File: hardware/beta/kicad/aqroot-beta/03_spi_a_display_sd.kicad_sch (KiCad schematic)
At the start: 0 parts

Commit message: AQROOT Beta: capture I2C, audio, IR, and SPI-A subsystems
Reconciles the active KiCad project from OneDrive into the canonical
repository. The four subsystem sheets existed here only as 169-byte
empty stubs; the real schematic capture had been done in the OneDrive
working copy.

Sheets brought in:
  03_spi_a_display_sd.kicad_sch   stub ->  62136 bytes
  05_i2c_devices.kicad_sch        stub ->  59631 bytes
  06_audio.kicad_sch              stub ->  55263 bytes
  07_ir.kicad_sch                 stub ->  50216 bytes

Also updated: aqroot-Beta.kicad_sch (root sheet, now carrying the
child sheet instances) and aqroot-Beta.kicad_pro.

03_spi_a_display_sd instantiates AQROOT_Beta:ILI9341_FT6236_MODULE_-
PLACEHOLDER; its cached symbol matches libraries/AQROOT_Beta.kicad_sym
exactly (13 pins, blank footprint, on_board=no).

Deliberately not taken from OneDrive:
  - sym-lib-table / fp-lib-table. The OneDrive copies hard-code an
    absolute P:/ path to this repository's library; the versions kept
    here use ${KIPRJMOD} and stay portable.
  - aqroot-Beta.kicad_prl (local project state) and .history/
    (2388 editor-history files, 5.87 MB).

Sheets identical on both sides and therefore untouched: 01_power_tree,
02_mcu_core, 04_spi_b_radios_nfc, 08_buttons_expanders,
09_community_header, aqroot-Beta.kicad_pcb.

Every copied file was verified by SHA-256 against its source, and each
staged blob is byte-identical to the working-tree file: CRLF endings
are preserved per .gitattributes, with no EOL normalization or
reformatting.

Co-Authored-By: Claude Opus 5 <noreply@anthropic.com>
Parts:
- added C13, C14: 100nF, symbol Device:C
- added C15: 10uF, symbol Device:C
- added J1: ILI9341_FT6236_MODULE_PLACEHOLDER, symbol AQROOT_Beta:ILI9341_FT6236_MODULE_PLACEHOLDER
- added J2: Micro_SD_Card, symbol Connector:Micro_SD_Card
- added R25, R26: 10k, symbol Device:R
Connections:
- new net +3V3: C13.1, C14.1, C15.1, J1.1 (VCC_3V3), J2.4 (VDD), R25.1, R26.1
- new net DISP_BL_CTL: J1.9 (LCD_BL_CTL)
- new net DISP_CS_N: J1.6 (LCD_CS_N), R26.2
- new net DISP_DC: J1.7 (LCD_DC)
- new net DISP_RST_N: J1.8 (LCD_RST_N)
- new net GND: C13.2, C14.2, C15.2, J1.2 (GND), J2.6 (VSS), J2.SH (SHIELD)
- new net I2C_SCL_INT: J1.11 (CTP_SCL)
- new net I2C_SDA_INT: J1.10 (CTP_SDA)
- new net SD_CS_N: J2.2 (DAT3/CD), R25.2
- new net SPI_A_MISO: J1.5 (LCD_MISO), J2.7 (DAT0)
- new net SPI_A_MOSI: J1.4 (LCD_MOSI), J2.3 (CMD)
- new net SPI_A_SCK: J1.3 (LCD_SCK), J2.5 (CLK)
- new net TOUCH_RST_N: J1.12 (CTP_RST_N)
- no-connect marks 0 -> 3
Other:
- note added: "DISPLAY FUNCTIONAL PLACEHOLDER ILI9341 SPI LCD + FT6236 TOUCH FT6236 EXPECTED I2C ADDRESS: 0x38 EXACT MODULE / CONNECTOR / PIN NUMBERING PENDING BACKLIGHT INTERFACE PENDING SUPPLY INTERFACE PENDING NO FOOTPRINT ASSIGNED DO NOT ROUTE"
- note added: "MICROSD SOCKET - FUNCTIONAL PLACEHOLDER SPI MODE: DAT3/CD = SD_CS_N CMD = SPI_A_MOSI CLK = SPI_A_SCK DAT0 = SPI_A_MISO DAT1 / DAT2 UNUSED CARD DETECT NOT IMPLEMENTED EXACT SOCKET / FOOTPRINT NOT SELECTED DO NOT ROUTE"

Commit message: AQROOT Beta: assign standard passive footprints
Assigns footprints to 40 passives whose package is unambiguous from
existing project precedent. Property-value edits only - no symbol, wire,
label or net touched.

  28 resistors -> Resistor_SMD:R_0603_1608Metric
     R1 R2 R3-R17 R18 R19 R20 R21 R22 R23 R25 R26 R27 R28 R29
     Basis: all 39 already-assigned resistors in the project are 0603, and
     every one of these is signal-level (pull-ups, dividers, series
     termination, MOSFET gate network).

  12 capacitors -> Capacitor_SMD:C_0603_1608Metric
     C1 C2 C4 C5 C6 C7 C8 C9 C13 C14 C16 C17
     Basis: 100nF is 5/5 and 1uF is 4/4 for 0603 among already-assigned
     capacitors - unanimous.

DELIBERATELY NOT ASSIGNED - split precedent, needs a decision:
  C3, C15, C10  10uF   -> project uses BOTH C_1206 (x2) and C_0805 (x1)
  C11           4.7uF  -> single 0805 precedent, different subsystem
Bulk capacitors must not be blindly converted to 0603, and the existing
precedent does not settle 0805 vs 1206.

Also untouched per instruction: C12/R24/Q1 (TBD), C18/C19 (placeholder),
L1/L2, mechanical switches and connectors, and the four RF/module
placeholders.

Separately noted, NOT changed here: C24 is 22uF 25V X7R with
C_0603_1608Metric already assigned. A 22uF 25V X7R does not exist in 0603
and the project's other 22uF parts use 1206/0805 - this looks like a
pre-existing error and is flagged for the BOM pass, not silently altered.

Verified with kicad-cli: netlist pin-to-net mapping byte-identical before
and after. ERC unchanged: raw 48, unique 24, excluded 24, real 0.
Footprint coverage 97 -> 137 of 166 components.

Co-Authored-By: Claude Opus 5 <noreply@anthropic.com>
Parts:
- C13, C14: footprint (none) -> Capacitor_SMD:C_0603_1608Metric
- R25, R26: footprint (none) -> Resistor_SMD:R_0603_1608Metric
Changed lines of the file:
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@@
 			)
 		)
-		(property "Footprint" ""
+		(property "Footprint" "Capacitor_SMD:C_0603_1608Metric"
 			(at 78.4352 64.77 0)
 			(hide yes)
@@
 			)
 		)
-		(property "Footprint" ""
+		(property "Footprint" "Resistor_SMD:R_0603_1608Metric"
 			(at 193.802 90.17 90)
 			(hide yes)
@@
 			)
 		)
-		(property "Footprint" ""
+		(property "Footprint" "Resistor_SMD:R_0603_1608Metric"
 			(at 205.232 90.17 90)
 			(hide yes)
@@
 			)
 		)
-		(property "Footprint" ""
+		(property "Footprint" "Capacitor_SMD:C_0603_1608Metric"
 			(at 228.2952 96.52 0)
 			(hide yes)

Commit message: AQROOT Beta: assign remaining generic bulk-cap footprints
Assigns Capacitor_SMD:C_0805_2012Metric to the four bulk capacitors left
open by the standard-passive pass.

  C3   10uF   +3V3                  02_mcu_core     generic bulk decoupling
  C15  10uF   +3V3                  03_spi_a        generic bulk decoupling
  C10  10uF   +3V3                  06_audio        generic bulk decoupling
  C11  4.7uF  /07_IR/IR_RX_VS_LOCAL 07_ir           TSOP382 supply RC

Basis: these are NOT regulator input/output capacitors. The project's 1206
precedent (C26/C27 CIN, C29-C32 COUT) is a TPS63020-specific requirement -
the kicad README states '1206 preferred ... Close to VIN/PGND' for those
parts only, so it does not generalise. For generic 10uF/10V and 4.7uF/10V
bulk on a 3.3V rail, 0805 is adequate and is the project's generic
precedent (C33, C20). C11's role is documented at libraries/README.md:1264
as Vishay's TSOP382 application R1/C1 supply filter, paired with R21 100R.

Property-value edits only - four lines. No value, symbol, wire, label or
net touched.

Verified with kicad-cli: netlist pin-to-net mapping byte-identical before
and after. ERC unchanged: raw 48, unique 24, excluded 24, real 0.

Still open and deliberately untouched: exact MPNs and DC-bias derating for
these parts. A 10uF/10V 0805 X7R typically retains only ~60-70% of its
nominal capacitance at 3.3V, so effective capacitance must be confirmed at
the BOM pass - the package is locked here, the part is not.

Co-Authored-By: Claude Opus 5 <noreply@anthropic.com>
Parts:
- C15: footprint (none) -> Capacitor_SMD:C_0805_2012Metric
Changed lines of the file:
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@@
 			)
 		)
-		(property "Footprint" ""
+		(property "Footprint" "Capacitor_SMD:C_0805_2012Metric"
 			(at 243.5352 96.52 0)
 			(hide yes)

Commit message: AQROOT Beta: lock mechanical component selections
Records exact MPN / manufacturer / package metadata for the mechanical
parts. All four footprints stay BLANK - every one needs a vendor drawing.

  SW9  JS102011SAQN     C&K (Littelfuse)      right-angle SMD SPDT slide
  J2   5025700893       Molex                 SMT push-push microSD, 8 contacts
  LS1  CMS-1535-058SP   Same Sky (CUI)        15 mm round 8 ohm solder-pad
  J1   Adafruit 2770    Adafruit              2.8in 240x320 + FT6236U cap touch

SW9 - SYMBOL/PART CONFLICT FOUND, NOT PAPERED OVER:
JS102011SAQN is a 3-terminal SPDT, but this instance uses Switch:SW_SPST
which has only two pins (A,B). Any correct land pattern for this part has
three signal pads plus mounting tabs, so symbol and footprint cannot agree
as they stand. The locked electrical intent is SPST (VINA -> switch -> EN,
never switching GND) and wiring an SPDT as SPST is fine, but the symbol has
to expose the unused throw so it can carry a no-connect. Swapping the symbol
is an approval-gated change and was deliberately NOT made. Recorded in the
part's Note so it cannot be missed at footprint time.

J1 is recorded as a VENDOR SKU lock, not a production MPN lock - Adafruit
can change panel manufacturer while preserving compatibility. Its Note
marks it a critical PCB/enclosure dependency and lists what is still needed:
the current Adafruit mechanical/FPC drawing, verification of the 50-pin
0.5 mm FPC pinout against the existing sheet architecture, and selection of
the separate mating FPC connector. The ~69 x 50 x 4 mm figure is flagged
approximate.

SW1-SW8 were deliberately left without MPNs. The class is locked (compact
SMD tactile) but the enclosure doc specifies only that there are seven
controls - D-pad, A and B - with no top-push versus side-push actuation
requirement recorded, so no per-reference MPN could be justified without
inventing a mechanical decision.

No fabricated dimensions, land patterns or ratings. Electrical circuits,
signal ar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
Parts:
- J1: MPN TBD -> Adafruit 2770; Manufacturer TBD -> Adafruit (vendor SKU - NOT a production manufacturer MPN); Note (none) -> CRITICAL PCB/ENCLOSURE DEPENDENCY. Adafruit may change pane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; Package (none) -> 2.8 inch 240x320 ILI9341-compatible panel with FT6236U-comp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
- J2: MPN (none) -> 5025700893; Manufacturer (none) -> Molex; Note (none) -> Signal architecture unchanged: 1-bit SPI mode, DAT1/DAT2 in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; Package (none) -> SMT push-push microSD socket, 8 contacts + shield - part LO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
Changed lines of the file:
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@@
+			)
+		)
+		(property "Note" "Signal architecture unchanged: 1-bit SPI mode, DAT1/DAT2 intentionally unconnected, shield to GND. VERIFY the Molex contact numbering against Connector:Micro_SD_Card pin numbering, and confirm card-entry clearance and push-push travel against the Field Slate enclosure before placement."
+			(at 234.95 60.96 0)
+			(hide yes)
+			(show_name no)
+			(do_not_autoplace no)
+			(effects
+				(font
+					(size 1.27 1.27)
+				)
+			)
+		)
+		(property "Package" "SMT push-push microSD socket, 8 contacts + shield - part LOCKED. Footprint BLOCKED: needs the official Molex recommended land pattern."
+			(at 234.95 60.96 0)
+			(hide yes)
+			(show_name no)
+			(do_not_autoplace no)
+			(effects
+				(font
+					(size 1.27 1.27)
+				)
+			)
+		)
+		(property "Manufacturer" "Molex"
+			(at 234.95 60.96 0)
+			(hide yes)
+			(show_name no)
+			(do_not_autoplace no)
+			(effects
+				(font
+					(size 1.27 1.27)
+				)
+			)
+		)
+		(property "MPN" "5025700893"
+			(at 234.95 60.96 0)
+			(hide yes)
+			(show_name no)
+			(do_not_autoplace no)
+			(effects
+				(font
+					(size 1.27 1.27)
+				)
 			)
 		)
@@
 			)
 		)
+		(property "Note" "CRITICAL PCB/ENCLOSURE DEPENDENCY. Adafruit may change panel manufacturer while preserving compatibility, so 2770 is a vendor SKU lock for the Beta prototype and must NOT be treated as a production MPN lock. Required before J1 can be drawn: the current Adafruit mechanical/FPC drawing, verification of the 50-pin 0.5 mm FPC pinout against this sheet's architecture, and selection of the exact mating FPC connector (which is a separate part with its own land pattern). Panel dimensions above are approximate and must be confirmed against the current drawing."
+			(at 101.6 90.17 0)
+			(hide yes)
+			(show_name no)
+			(do_not_autoplace no)
+			(effects
+				(font
+					(size 1.27 1.27)
+				)
+			)
+		)
+		(property "Package" "2.8 inch 240x320 ILI9341-compatible panel with FT6236U-compatible capacitive touch, 50-pin 0.5 mm FPC, approx 69 x 50 x 4 mm - BETA PROTOTYPE LOCK ONLY. Footprint BLOCKED."
+			(at 101.6 90.17 0)
+			(hide yes)
+			(show_name no)
+			(do_not_autoplace no)
+			(effects
+				(font
+					(size 1.27 1.27)
+				)
+			)
+		)
 		(property "Description" "Functional placeholder for AQROOT Beta 2.8-inch ILI9341 SPI LCD with FT6236 capacitive touch"
 			(at 101.6 90.17 0)
@@
 			)
 		)
-		(property "Manufacturer" "TBD"
+		(property "Manufacturer" "Adafruit (vendor SKU - NOT a production manufacturer MPN)"
 			(at 101.6 90.17 0)
 			(hide yes)
@@
 			)
 		)
-		(property "MPN" "TBD"
+		(property "MPN" "Adafruit 2770"
 			(at 101.6 90.17 0)
 			(hide yes)

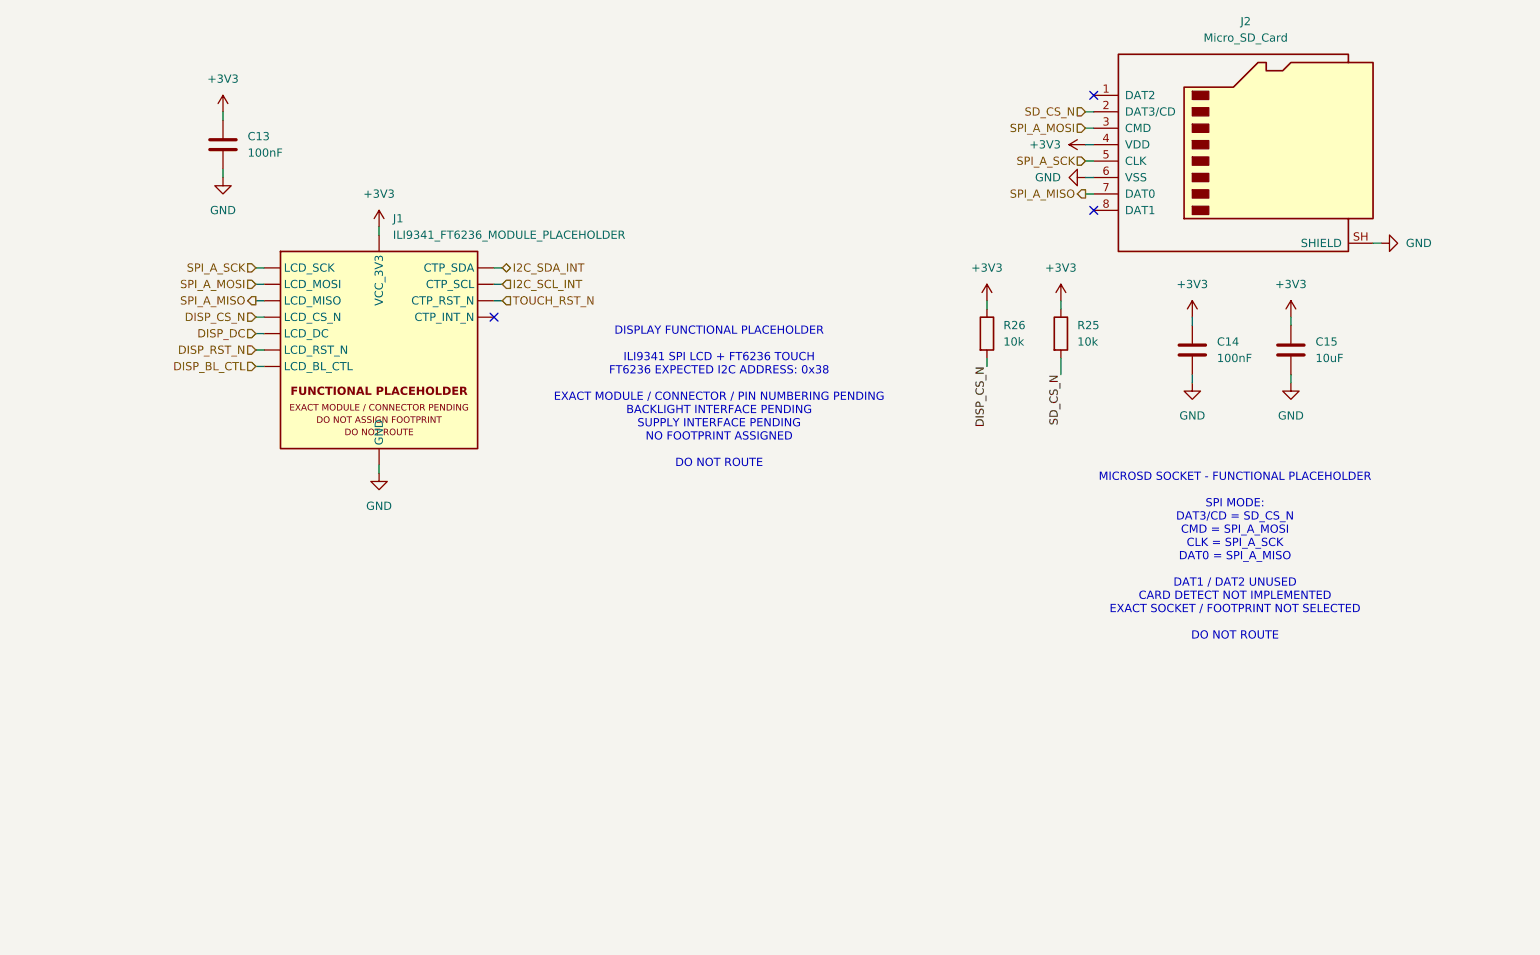
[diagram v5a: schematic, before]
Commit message: AQROOT Beta: capture physical 50-pin display interface and backlight driver
Replaces the 13-pin ILI9341_FT6236_MODULE_PLACEHOLDER with the real 50-contact
CH280QV10_CT_50P panel interface on the Hirose FH69 footprint, and adds the
dedicated TPS61169 backlight stage. Sheet paper A4 to A3 to fit the 66 mm-tall
symbol.

Committed as ONE change rather than the two requested. Splitting was not
possible without a broken intermediate: the backlight's LED_A1..A4 and LED_K
nets terminate on J1, so committing the driver first leaves those labels
dangling, while committing J1 first leaves DISP_BL_CTL and the LED nets
dangling. Either order fails the "ERC 0 before each commit" gate and would have
meant committing a half-wired J1.

BACKLIGHT COMPONENTS. U17 TPS61169DCKR on SOT-353_SC-70-5, classified
VERIFIED_IPC_ALTERNATE and not vendor-exact. L3 Coilcraft XFL4020-472MEC,
4.7 uH +/-20 percent, Isat 2 A, Irms 5 A, DCR 0.05 ohm max, AEC-Q200, reusing
the existing VERIFIED_VENDOR_EXACT Coilcraft_XFL4020 land pattern already shared
with L1 - deliberately oversized at about 11x the 181 mA peak, accepted to avoid
introducing a new unverified footprint and to consolidate on one inductor
family. D8 onsemi NSR0240V2T5G in SOD-323, the part TI names explicitly. C43 is
4.7 uF 16 V X7R 0805, chosen over 6.3 V 0603 so effective capacitance survives
3.3 V DC bias. C44 is 1 uF 50 V X7R 0805, rated against the 36 to 39 V open-LED
OVP threshold rather than the 4.2 V normal output. R69 RSET 2.55 ohm 1 percent,
R70 to R73 ballast 39 ohm 1 percent.

TOPOLOGY VERIFIED FROM THE NETLIST, not from intent. BL_SW carries U17 SW, L3
pin 2 and the D8 anode. LED_BOOST carries the D8 cathode, C44 and all four
ballasts. LED_A1 to LED_A4 each carry exactly one J1 anode and one ballast, so
the four branches stay independent. LED_K carries J1 pin 1, RSET and U17 FB.
DISP_BL_CTL reaches only U1 pin 24 and U17 CTRL, so no GPIO carries LED current.
Nothing touches NFC_5V_PA, TPS61023 or BAT_PROTECTED_P. Firmware c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
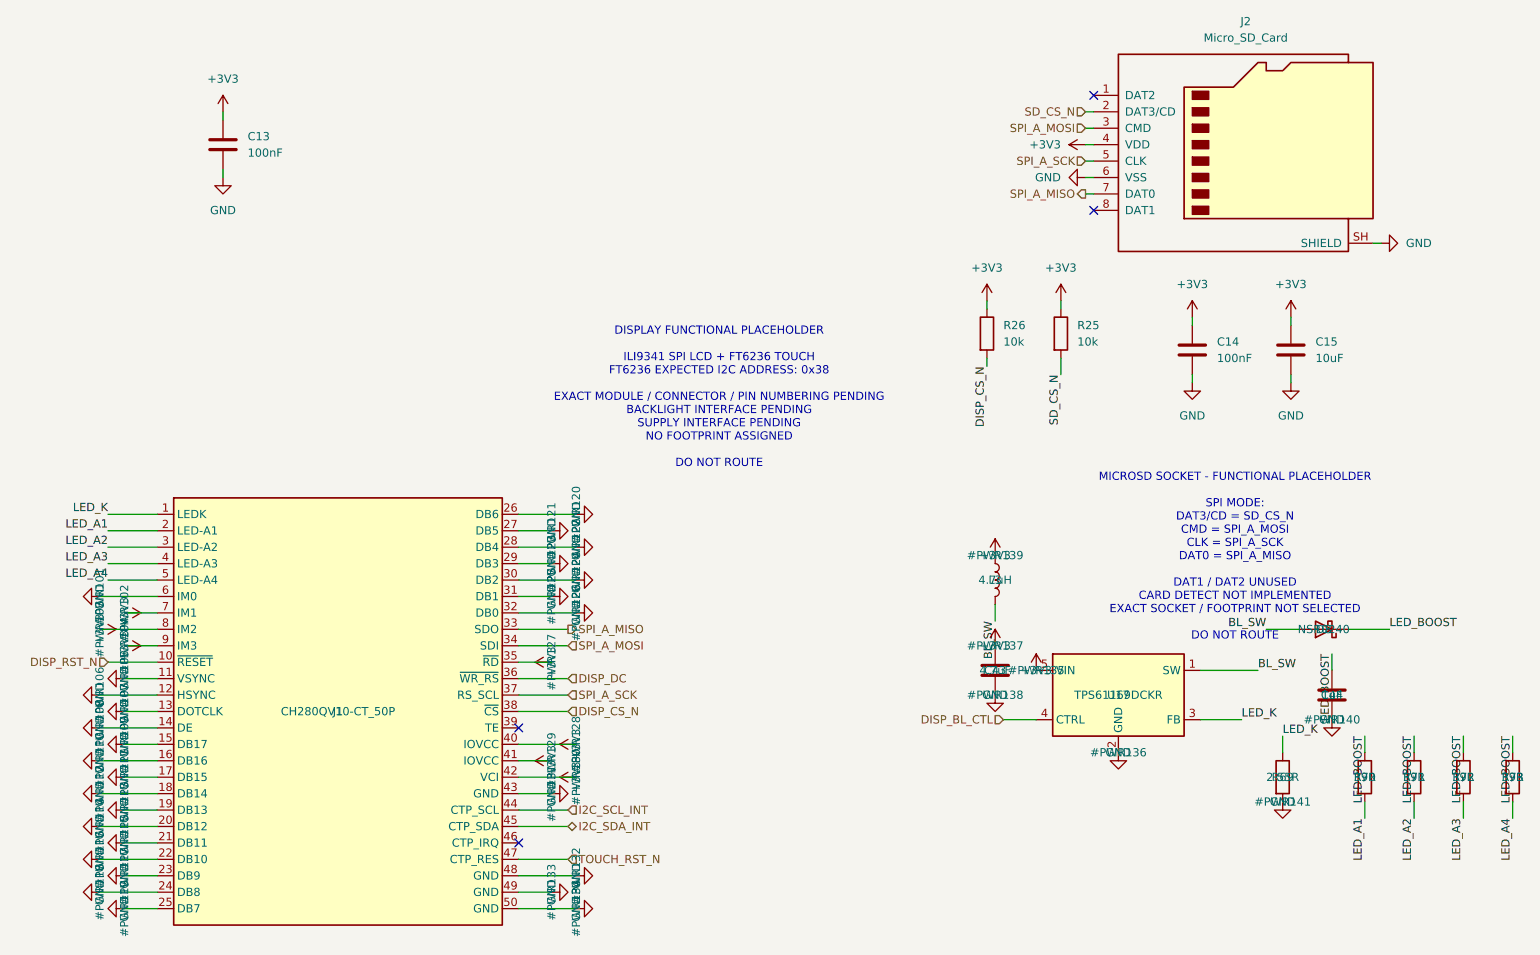
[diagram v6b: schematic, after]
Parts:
- removed J1: ILI9341_FT6236_MODULE_PLACEHOLDER, symbol AQROOT_Beta:ILI9341_FT6236_MODULE_PLACEHOLDER
- added C43: 4.7uF, Capacitor_SMD:C_0805_2012Metric, symbol Device:C
- added C44: 1uF, Capacitor_SMD:C_0805_2012Metric, symbol Device:C
- added D8: NSR0240, Diode_SMD:D_SOD-323, symbol Device:D_Schottky
- added J1: CH280QV10-CT_50P, AQROOT_Beta:Hirose_FH69-50S-0.5SH, symbol AQROOT_Beta:CH280QV10_CT_50P
- added L3: 4.7uH, AQROOT_Beta:Coilcraft_XFL4020, symbol Device:L
- added R69: 2.55R, Resistor_SMD:R_0603_1608Metric, symbol Device:R
- added R70, R71, R72, R73: 39R, Resistor_SMD:R_0603_1608Metric, symbol Device:R
- added U17: TPS61169DCKR, Package_TO_SOT_SMD:SOT-353_SC-70-5, symbol AQROOT_Beta:TPS61169DCKR
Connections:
- net +3V3: now also C43.1, J1.35 (~{RD}), J1.40 (IOVCC), J1.41 (IOVCC), J1.42 (VCI), J1.7 (IM1), J1.8 (IM2), J1.9 (IM3), L3.1, U17.5 (VIN)
- net DISP_BL_CTL: now also U17.4 (CTRL)
- net DISP_CS_N: now also J1.38 (~{CS})
- net DISP_DC: now also J1.36 (~{WR_RS})
- net DISP_RST_N: now also J1.10 (~{RESET})
- net GND: now also C43.2, C44.2, J1.11 (VSYNC), J1.12 (HSYNC), J1.13 (DOTCLK), J1.14 (DE), J1.15 (DB17), J1.16 (DB16), J1.17 (DB15), J1.18 (DB14), J1.19 (DB13), J1.20 (DB12), J1.21 (DB11), J1.22 (DB10), J1.23 (DB9), J1.24 (DB8), J1.25 (DB7), J1.26 (DB6), J1.27 (DB5), J1.28 (DB4), J1.29 (DB3), J1.30 (DB2), J1.31 (DB1), J1.32 (DB0), J1.43 (GND), J1.48 (GND), J1.49 (GND), J1.50 (GND), J1.6 (IM0), R69.2, U17.2 (GND)
- net I2C_SCL_INT: now also J1.44 (CTP_SCL)
- net I2C_SDA_INT: now also J1.45 (CTP_SDA)
- net SPI_A_MISO: now also J1.33 (SDO)
- net SPI_A_MOSI: now also J1.34 (SDI)
- net SPI_A_SCK: now also J1.37 (RS_SCL)
- net TOUCH_RST_N: now also J1.47 (CTP_RES)
- new net BL_SW: D8.2 (A), L3.2, U17.1 (SW)
- new net LED_A1: J1.2 (LED-A1), R70.2
- new net LED_A2: J1.3 (LED-A2), R71.2
- new net LED_A3: J1.4 (LED-A3), R72.2
- new net LED_A4: J1.5 (LED-A4), R73.2
- new net LED_BOOST: C44.1, D8.1 (K), R70.1, R71.1, R72.1, R73.1
- new net LED_K: J1.1 (LEDK), R69.1, U17.3 (FB)
- no-connect marks 3 -> 4
